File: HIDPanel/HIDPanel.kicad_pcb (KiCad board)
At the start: 2 copper layers, 116.8 x 127 mm, 47 parts, among them J1 2PosTerminal, M1 ModulePlug, M10 ModulePlug, M11 ModulePlug, M12 ModulePlug, M13 ModulePlug, M14 ModulePlug, M15 ModulePlug, M2 ModulePlug, M3 ModulePlug, M4 ModulePlug, M5 ModulePlug, M6 ModulePlug, M7 ModulePlug, M8 ModulePlug, M9 ModulePlug, Q1 2N3904, U1 Pico, U2 74HCT08, U3 4051, U4 4051, U5 4051, U6 TL431LP

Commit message: Tweaked some distances
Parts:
- renumbered M3 to M1, M9 to M11, M15 to M13, M13 to M15, M1 to M3, M7 to M5, M5 to M7, M11 to M9

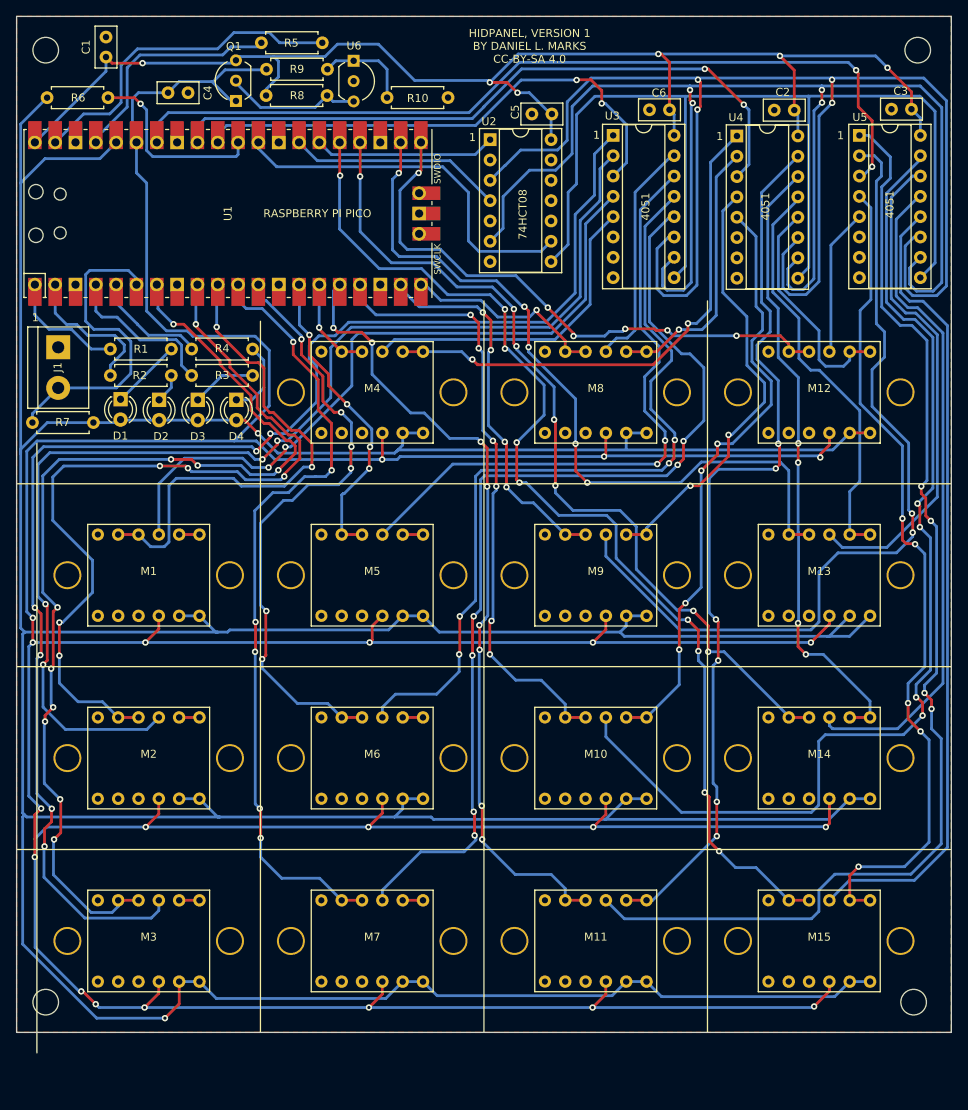
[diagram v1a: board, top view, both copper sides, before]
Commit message: Spaced out plugin footprint bigger
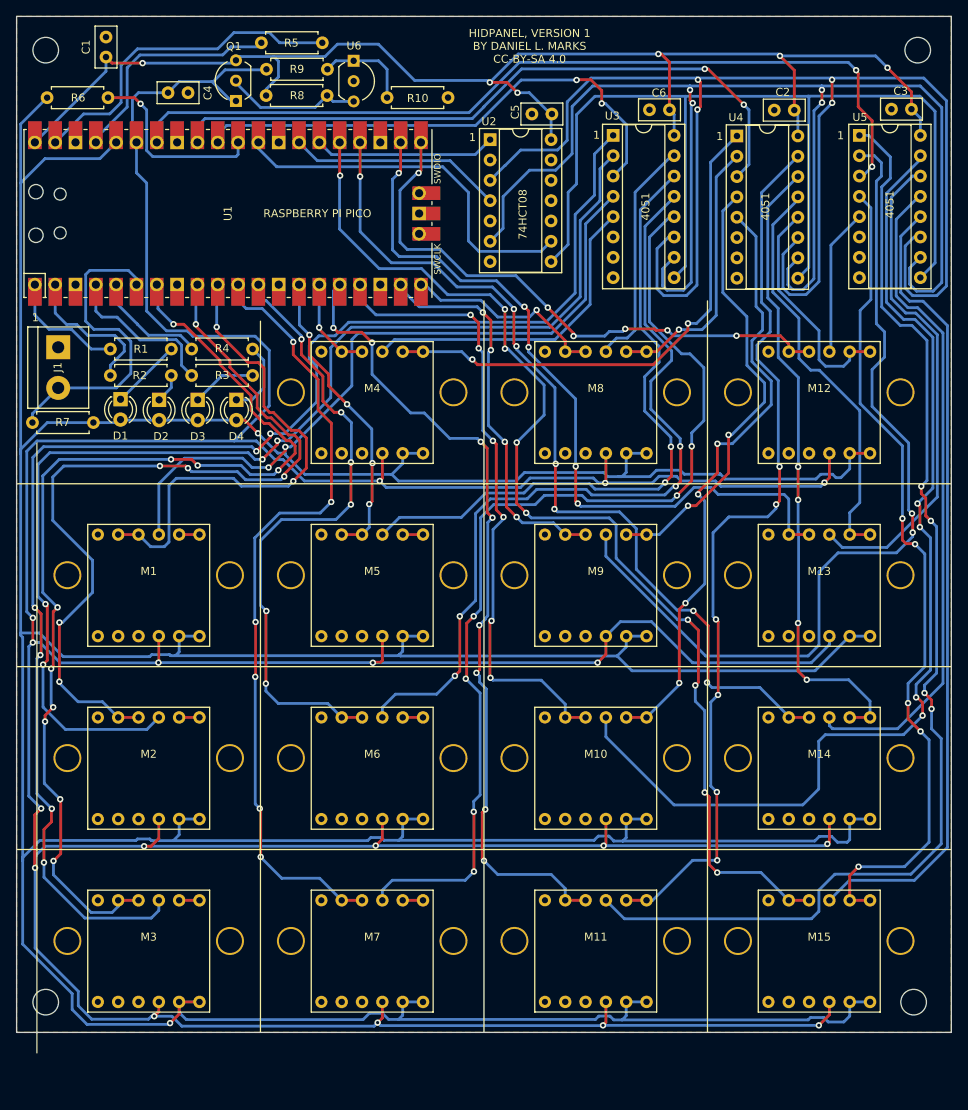
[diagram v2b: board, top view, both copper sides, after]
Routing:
- net +3.3V: track 608.3 -> 633.8 mm
- net M11A: track 106.7 -> 111.0 mm
- net SW1M13: track 136.1 -> 139.9 mm
- net SW1M14: track 108.0 -> 111.7 mm
- net ACC: track 603.0 -> 606.6 mm, vias 21 -> 18
- net M5A: track 124.0 -> 127.3 mm
- net M7A: track 79.0 -> 82.1 mm
- net SW1M9: track 100.2 -> 102.7 mm
- net SW1M10: track 76.7 -> 79.2 mm
- net SW1M6: track 76.7 -> 78.9 mm
- net M10A: track 133.2 -> 131.3 mm
- net SW2M14: track 78.4 -> 80.1 mm
- net SW1M11: track 47.6 -> 49.1 mm
- net SW1M7: track 39.2 -> 38.1 mm
- net SW1M3: track 63.3 -> 62.4 mm
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
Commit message: Minor layout tweaks
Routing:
- net +3.3V: track 633.8 -> 624.5 mm
- net ACC: track 606.6 -> 609.5 mm, vias 18 -> 14

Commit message: Oops 74HCT32 not 74HCT08
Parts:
- U2: value 74HCT08 -> 74HCT32
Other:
- board text added: "74HCT32"
- board text removed: "74HCT08"
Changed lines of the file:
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@@
       (effects (font (size 1 1) (thickness 0.15)))
     )
-    (fp_text value "74HCT08" (at 3.81 17.57) (layer "F.Fab")
+    (fp_text value "74HCT32" (at 3.81 17.57) (layer "F.Fab")
       (effects (font (size 1 1) (thickness 0.15)))
     )
@@
     (effects (font (size 1 1) (thickness 0.15)))
   )
-  (gr_text "74HCT08" (at 149.64 42.53 90) (layer "F.SilkS")
-    (effects (font (size 1 1) (thickness 0.15)))
-  )
+  (gr_text "74HCT32" (at 149.64 42.53 90) (layer "F.SilkS")
+    (effects (font (size 1 1) (thickness 0.15)))
+  )

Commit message: Added CAD models
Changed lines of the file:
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@@
     (property "Sheetname" "")
     (attr through_hole)
-    (fp_text reference "C5" (at 4.6 0.25 90) (layer "F.SilkS")
+    (fp_text reference "C5" (at 1.27 2.23 180) (layer "F.SilkS")
       (effects (font (size 1 1) (thickness 0.15)))
     )

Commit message: Rev 2 HIDPanel board
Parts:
- added JP1: Jumper_3_Bridged12, Jumper:SolderJumper-3_P1.3mm_Bridged2Bar12_Pad1.0x1.5mm, F.Cu at (146.5, 27.1)
- J1: footprint TerminalBlock:TerminalBlock_bornier-2_P5.08mm -> Connector_PinHeader_2.54mm:PinHeader_1x02_P2.54mm_Vertical
- U2: value 74HCT32 -> 74HCT00
- moved J1 17.2 mm to (104.8, 70.2)
- moved R3 11.4 mm to (106.0, 57.0)
- moved R7 10.7 mm to (98.9, 70.2), turned to 180 degrees
- moved R2 9.97 mm to (96.0, 60.1)
- moved R1 9.93 mm to (96.1, 56.9)
- moved R4 9.83 mm to (106.1, 60.1)
- moved H3 7.00 mm to (198.5, 148.0)
- moved H4 7.00 mm to (90.0, 148.0)
- moved D4 5.19 mm to (109.5, 62.9)
- moved D3 5.15 mm to (104.7, 62.9)
- moved D2 5.05 mm to (100.0, 63.0)
- moved D1 4.94 mm to (95.2, 62.9)
- moved R10 4.61 mm to (132.3, 23.3)
- moved C4 3.96 mm to (106.7, 23.6)
- moved U6 1.90 mm to (128.4, 21.4)
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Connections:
- U2 pad 10: GND -> Net-(U2-Pad10)
- U2 pad 2: GND -> Net-(U2-Pad10)
- U2 pad 5: GND -> Net-(U2-Pad10)
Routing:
- net Net-(U2-Pad10): track 0.00 -> 28.6 mm, vias 0 -> 1
- net +5V: track 168.3 -> 189.6 mm
- net +3.3V: track 624.5 -> 639.4 mm
- net Net-(J1-Pad2): track 39.8 -> 25.9 mm
- net LED2: track 20.1 -> 7.64 mm
- net LED0: track 15.0 -> 6.79 mm
- net SW1M2: track 102.8 -> 95.4 mm
- net LED1: track 18.4 -> 12.3 mm
- net M1A: track 176.6 -> 170.7 mm
- net M2A: track 147.7 -> 141.9 mm
- net SEL2: track 46.8 -> 52.2 mm
- net SW1M1: track 130.3 -> 125.3 mm
- net Net-(D4-Pad1): track 9.49 -> 4.56 mm
- net SW1M3: track 62.4 -> 59.3 mm
- net LED3: track 14.3 -> 11.5 mm
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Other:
- board size 116.8 x 127 mm -> 116.8 x 134.6 mm
- board text added: "74HCT00"
- board text added: "HIDPANEL, VERSION 2 BY DANIEL L. MARKS CC-BY-SA 4.0"
- board text added: "SW2 NOT CONNECTED"
- board text removed: "74HCT32"
- board text removed: "HIDPANEL, VERSION 1 BY DANIEL L. MARKS CC-BY-SA 4.0"

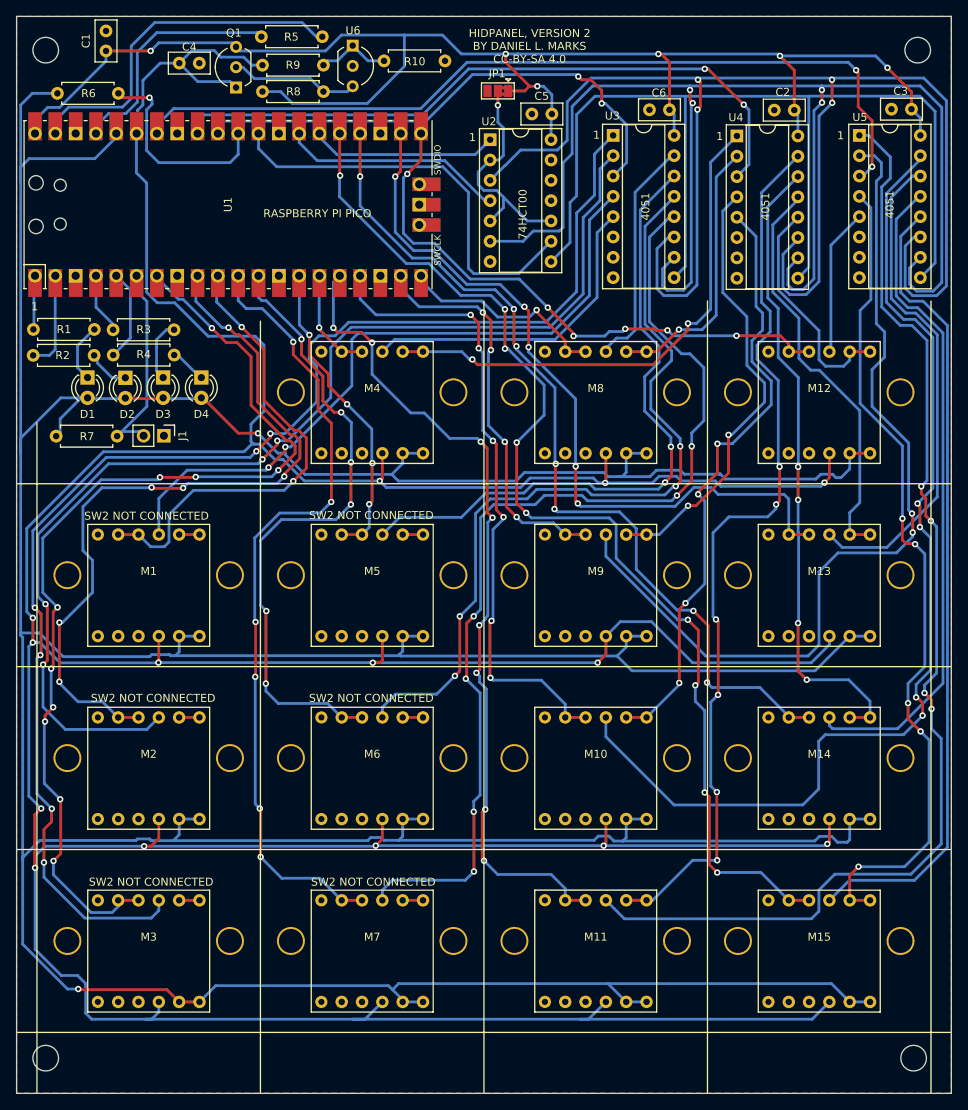
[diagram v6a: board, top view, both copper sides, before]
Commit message: A few layout tweaks
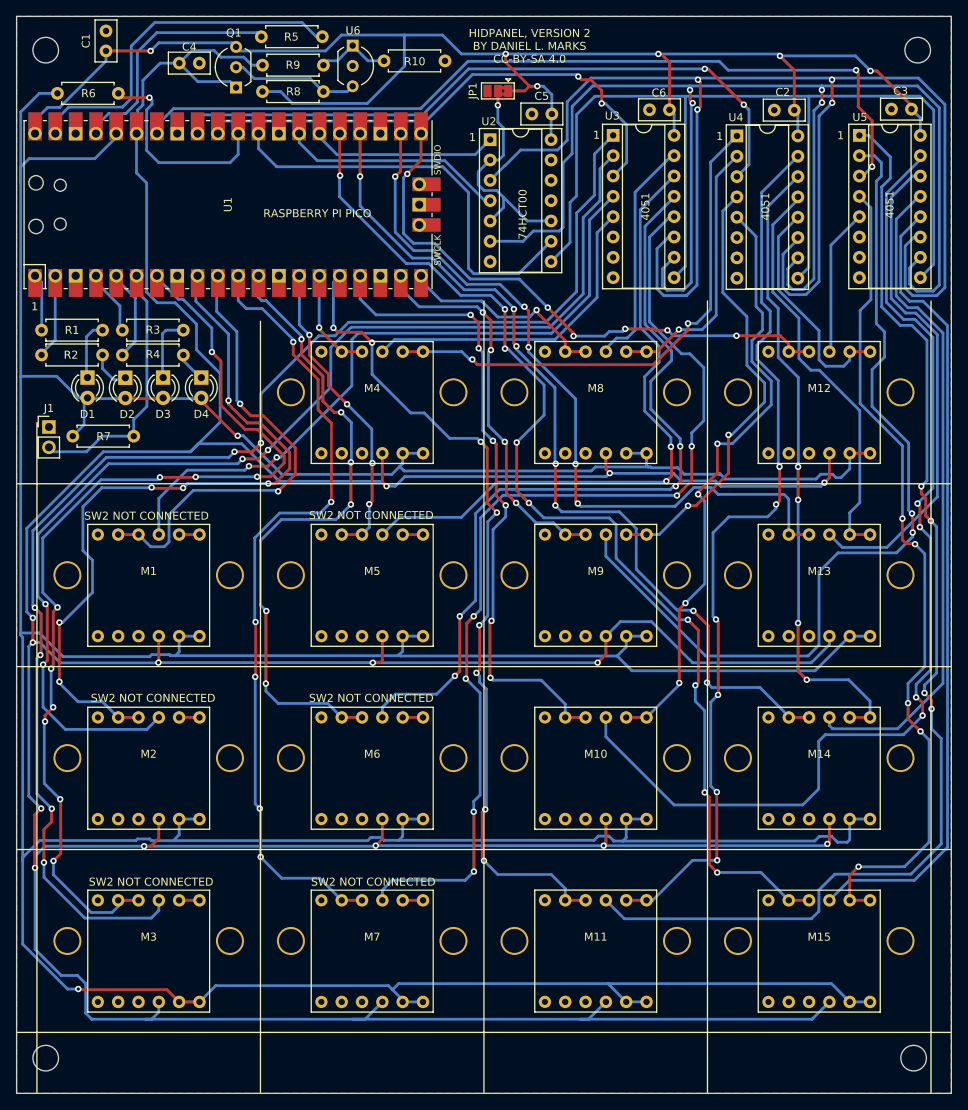
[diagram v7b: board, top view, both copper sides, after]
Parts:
- moved J1 14.4 mm to (90.4, 69.1), turned to 0 degrees
- moved R7 2.08 mm to (101.0, 70.2)
- moved R3 1.16 mm to (107.2, 57.0)
- moved R4 1.14 mm to (107.2, 60.1)
- moved R2 1.05 mm to (97.1, 60.1)
- moved R1 1.02 mm to (97.1, 57.0)
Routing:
- net +3.3V: track 639.4 -> 632.1 mm
- net Net-(J1-Pad2): track 25.9 -> 32.9 mm
- net ACC: track 607.0 -> 602.4 mm
- net M1A: track 170.7 -> 168.6 mm
- net LED1: track 12.3 -> 10.6 mm
- net SW1M1: track 125.3 -> 123.9 mm
- net SW1M2: track 95.4 -> 94.1 mm
- net M2A: track 141.9 -> 140.9 mm
- net +5V: track 189.6 -> 188.6 mm
- net SW1M11: track 50.2 -> 49.2 mm
- net SW1M13: track 138.6 -> 137.7 mm
- net SW1M3: track 59.3 -> 58.5 mm
- net Net-(D4-Pad1): track 4.56 -> 3.82 mm
- net M6A: track 102.4 -> 101.8 mm
- net M7A: track 82.1 -> 81.5 mm
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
